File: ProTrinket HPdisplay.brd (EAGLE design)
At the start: 17.8 x 37.3 mm, 17 parts

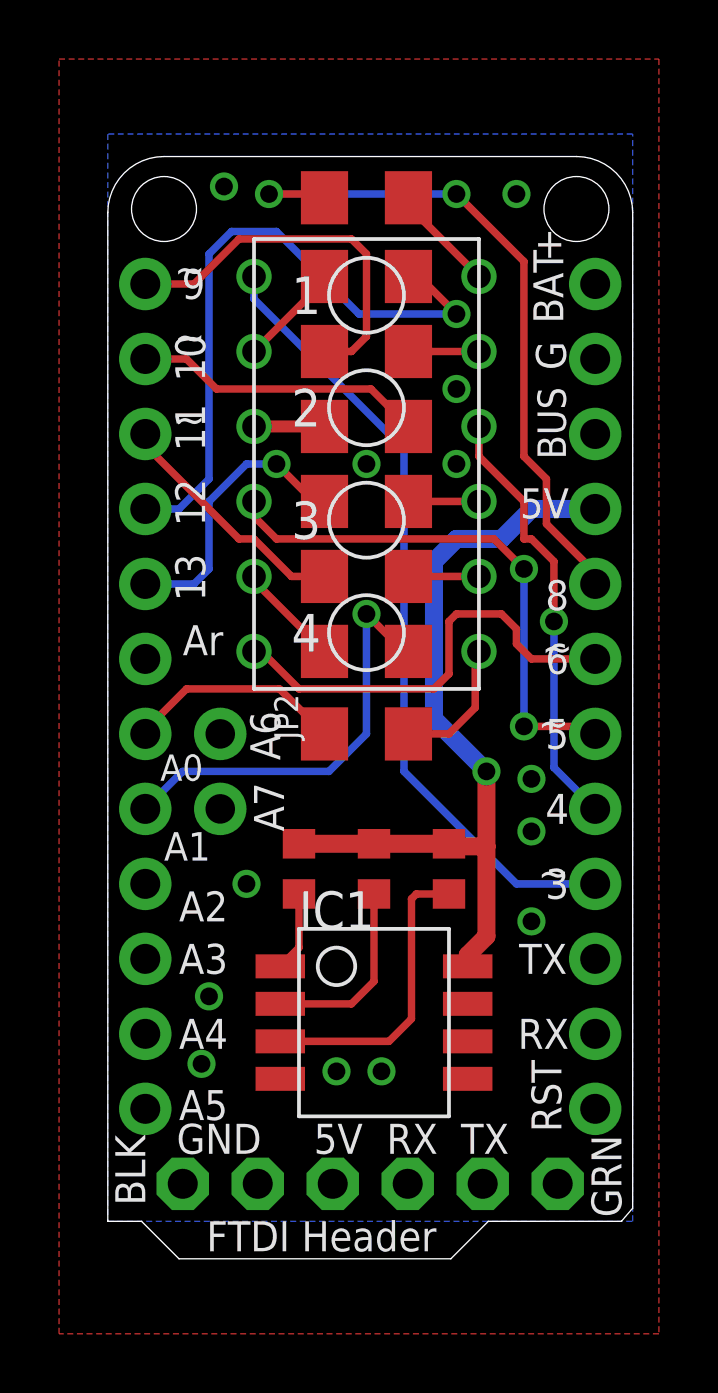
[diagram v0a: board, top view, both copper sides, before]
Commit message: fixed IIC connection
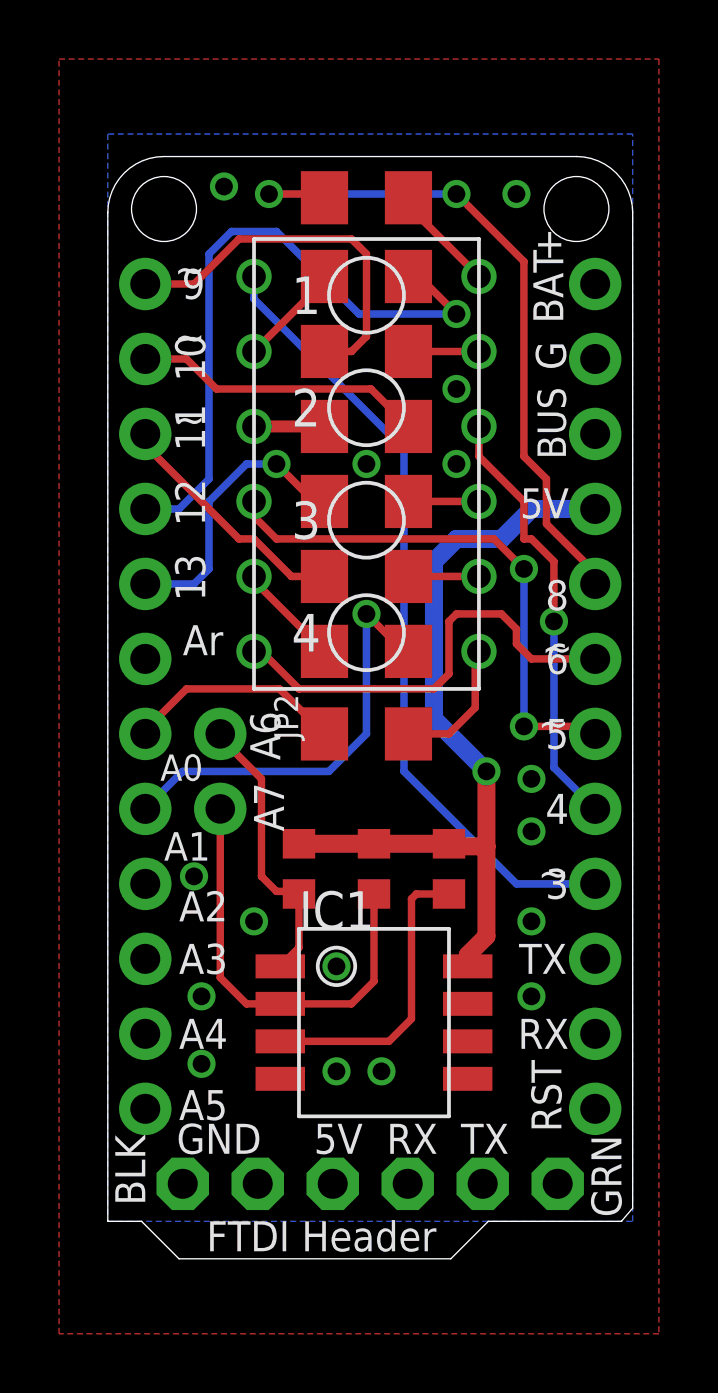
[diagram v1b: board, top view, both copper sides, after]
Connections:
- removed net N$10: IC1.2, R10.2
- removed net N$13: IC1.1, R9.2
- new net A6: IC1.1, JP2.1, R9.2
- new net A7: IC1.2, JP2.2, R10.2
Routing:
- net A7: track 0.00 -> 14.6 mm
- net A6: track 0.00 -> 9.64 mm
- net N$10: track 6.45 -> 0.00 mm
- net N$13: track 2.72 -> 0.00 mm
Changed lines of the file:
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@@
 <layer number="2" name="Route2" color="1" fill="3" visible="no" active="yes"/>
 <layer number="3" name="Route3" color="4" fill="3" visible="no" active="yes"/>
-<layer number="4" name="Route4" color="1" fill="4" visible="no" active="yes"/>
+<layer number="4" name="Route4" color="1" fill="4" visible="yes" active="yes"/>
 <layer number="5" name="Route5" color="4" fill="4" visible="no" active="yes"/>
 <layer number="6" name="Route6" color="1" fill="8" visible="no" active="yes"/>
@@
 <vertex x="12.7" y="33.02"/>
 </polygon>
-<via x="19.05" y="48.26" extent="1-16" drill="0.6"/>
+<via x="17.272" y="48.514" extent="1-16" drill="0.6"/>
 <via x="22.098" y="41.91" extent="1-16" drill="0.6"/>
 <via x="28.702" y="50.038" extent="1-16" drill="0.6"/>
-<via x="17.78" y="44.45" extent="1-16" drill="0.6"/>
+<via x="17.526" y="44.45" extent="1-16" drill="0.6"/>
 <via x="17.526" y="42.164" extent="1-16" drill="0.6"/>
 <via x="28.702" y="46.99" extent="1-16" drill="0.6"/>
@@
 <via x="26.162" y="62.484" extent="1-16" drill="0.6"/>
 <via x="23.114" y="62.484" extent="1-16" drill="0.6"/>
+<via x="19.304" y="46.99" extent="1-16" drill="0.6"/>
+<via x="22.098" y="45.466" extent="1-16" drill="0.6"/>
+<via x="28.702" y="44.45" extent="1-16" drill="0.6"/>
 </signal>
 <signal name="VBUS" class="1">
@@
 <wire x1="19.304" y1="58.522" x2="21.692" y2="56.134" width="0.254" layer="1"/>
 </signal>
-<signal name="N$10">
+<signal name="A7">
 <contactref element="IC1" pad="2"/>
 <contactref element="R10" pad="2"/>
@@
 <wire x1="23.368" y1="44.958" x2="22.606" y2="44.196" width="0.254" layer="1"/>
 <wire x1="22.606" y1="44.196" x2="20.193" y2="44.196" width="0.254" layer="1"/>
+<contactref element="JP2" pad="2"/>
+<wire x1="18.161" y1="50.8" x2="18.161" y2="45.085" width="0.254" layer="1"/>
+<wire x1="18.161" y1="45.085" x2="19.05" y2="44.196" width="0.254" layer="1"/>
+<wire x1="19.05" y1="44.196" x2="20.193" y2="44.196" width="0.254" layer="1"/>
 </signal>
 <signal name="N$11">
@@
 <wire x1="23.876" y1="42.926" x2="20.193" y2="42.926" width="0.254" layer="1"/>
 </signal>
-<signal name="N$13">
+<signal name="A6">
+<contactref element="JP2" pad="1"/>
 <contactref element="IC1" pad="1"/>
 <contactref element="R9" pad="2"/>
 <wire x1="20.828" y1="47.918" x2="20.828" y2="46.101" width="0.254" layer="1"/>
 <wire x1="20.828" y1="46.101" x2="20.193" y2="45.466" width="0.254" layer="1"/>
+<wire x1="18.161" y1="53.34" x2="18.161" y2="53.213" width="0.254" layer="1"/>
+<wire x1="18.161" y1="53.213" x2="19.558" y2="51.816" width="0.254" layer="1"/>
+<wire x1="19.558" y1="51.816" x2="19.558" y2="48.514" width="0.254" layer="1"/>
+<wire x1="19.558" y1="48.514" x2="20.066" y2="48.006" width="0.254" layer="1"/>
+<wire x1="20.066" y1="48.006" x2="20.74" y2="48.006" width="0.254" layer="1"/>
+<wire x1="20.74" y1="48.006" x2="20.828" y2="47.918" width="0.254" layer="1"/>
 </signal>
 </signals>

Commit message: removed vias
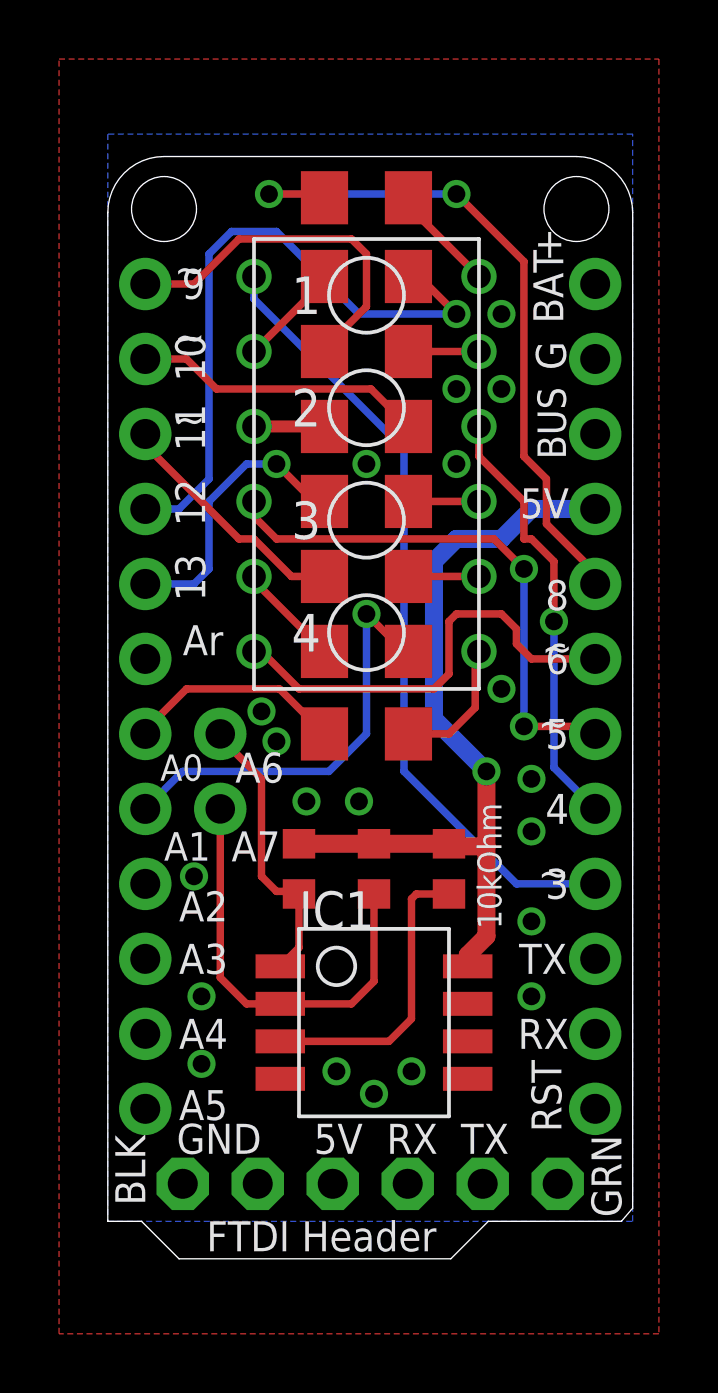
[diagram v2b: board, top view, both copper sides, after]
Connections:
- net GND: now also FTDI.2
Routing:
- net D9: track 12.8 -> 12.2 mm
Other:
- board text added: "10kOhm"
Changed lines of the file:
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@@
 <text x="16.764" y="45.72" size="1.016" layer="21" font="vector" ratio="10" rot="R180" align="center-right">A3</text>
 <text x="16.764" y="47.498" size="1.016" layer="21" font="vector" ratio="10" rot="R180" align="center-right">A2</text>
-<text x="19.812" y="50.038" size="1.016" layer="21" font="vector" ratio="10" rot="R270" align="center-right">A7</text>
+<text x="18.542" y="49.53" size="1.016" layer="21" font="vector" ratio="10" rot="R180" align="center-right">A7</text>
 <text x="16.256" y="49.53" size="0.9652" layer="21" font="vector" ratio="10" rot="R180" align="center-right">A1</text>
 <text x="16.129" y="52.197" size="0.889" layer="21" font="vector" ratio="10" rot="R180" align="center-right">A0</text>
-<text x="19.685" y="52.451" size="1.016" layer="21" font="vector" ratio="10" rot="R270" align="center-right">A6</text>
+<text x="18.669" y="52.197" size="1.016" layer="21" font="vector" ratio="10" rot="R180" align="center-right">A6</text>
 <text x="16.891" y="56.515" size="1.016" layer="21" font="vector" ratio="10" rot="R180" align="center-right">Ar</text>
 <text x="17.145" y="59.436" size="1.016" layer="21" font="vector" ratio="10" rot="R90" align="center-right">13</text>
@@
 <text x="21.59" y="36.322" size="1.016" layer="21" font="vector" ratio="12" align="center">FTDI Header</text>
 <text x="24.13" y="53.848" size="1.27" layer="26" font="vector" rot="MR90">#IStandWithAhmed</text>
+<text x="27.686" y="46.736" size="0.8128" layer="21" font="vector" rot="R90">10kOhm</text>
 </plain>
 <attributes>
@@
 </element>
 <element name="JP2" library="microbuilder" package="1X02_ROUND" value="" x="18.161" y="52.07" smashed="yes" rot="R270">
-<attribute name="NAME" x="19.9898" y="54.6862" size="0.8128" layer="25" ratio="18" rot="R270"/>
 <attribute name="VALUE" x="14.986" y="54.61" size="0.4064" layer="27" ratio="10" rot="R270"/>
 </element>
@@
 </element>
 <element name="R8" library="rcl" package="R1206" value="680Ohm" x="23.114" y="56.134" smashed="yes">
-<attribute name="VALUE" x="21.082" y="50.546" size="1.27" layer="27" font="vector"/>
+<attribute name="VALUE" x="26.416" y="52.578" size="0.8128" layer="27" font="vector" rot="R90"/>
 </element>
 <element name="IC1" library="lm75" package="SO8_LM75" value="" x="23.368" y="44.196" rot="R270"/>
@@
 <contactref element="IC1" pad="5"/>
 <contactref element="IC1" pad="4"/>
-<via x="23.622" y="41.91" extent="1-16" drill="0.6"/>
+<via x="24.638" y="41.91" extent="1-16" drill="0.6"/>
 <polygon width="0.4064" layer="1">
 <vertex x="12.7" y="76.2"/>
@@
 <via x="28.702" y="51.816" extent="1-16" drill="0.6"/>
 <via x="26.162" y="65.024" extent="1-16" drill="0.6"/>
-<via x="28.194" y="71.628" extent="1-16" drill="0.6"/>
-<via x="18.288" y="71.882" extent="1-16" drill="0.6"/>
 <via x="26.162" y="62.484" extent="1-16" drill="0.6"/>
 <via x="23.114" y="62.484" extent="1-16" drill="0.6"/>
-<via x="19.304" y="46.99" extent="1-16" drill="0.6"/>
-<via x="22.098" y="45.466" extent="1-16" drill="0.6"/>
 <via x="28.702" y="44.45" extent="1-16" drill="0.6"/>
+<via x="23.368" y="41.148" extent="1-16" drill="0.6"/>
+<contactref element="FTDI" pad="2"/>
+<via x="27.686" y="67.564" extent="1-16" drill="0.6"/>
+<via x="27.686" y="65.024" extent="1-16" drill="0.6"/>
+<via x="27.686" y="54.864" extent="1-16" drill="0.6"/>
+<via x="19.558" y="54.102" extent="1-16" drill="0.6"/>
+<via x="21.082" y="51.054" extent="1-16" drill="0.6"/>
+<via x="22.86" y="51.054" extent="1-16" drill="0.6"/>
+<via x="20.066" y="53.086" extent="1-16" drill="0.6"/>
 </signal>
 <signal name="VBUS" class="1">
@@
 <wire x1="18.796" y1="70.104" x2="22.606" y2="70.104" width="0.254" layer="1"/>
 <wire x1="22.606" y1="70.104" x2="23.114" y2="69.596" width="0.254" layer="1"/>
-<wire x1="23.114" y1="69.596" x2="23.114" y2="66.802" width="0.254" layer="1"/>
-<wire x1="23.114" y1="66.802" x2="22.606" y2="66.294" width="0.254" layer="1"/>
-<wire x1="22.606" y1="66.294" x2="21.692" y2="66.294" width="0.254" layer="1"/>
+<wire x1="23.114" y1="69.596" x2="23.114" y2="67.818" width="0.254" layer="1"/>
+<wire x1="23.114" y1="67.818" x2="22.352" y2="67.056" width="0.254" layer="1"/>
+<wire x1="22.352" y1="67.056" x2="21.692" y2="66.294" width="0.254" layer="1"/>
 </signal>
 <signal name="AREF">

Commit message: mixed up IIC lines
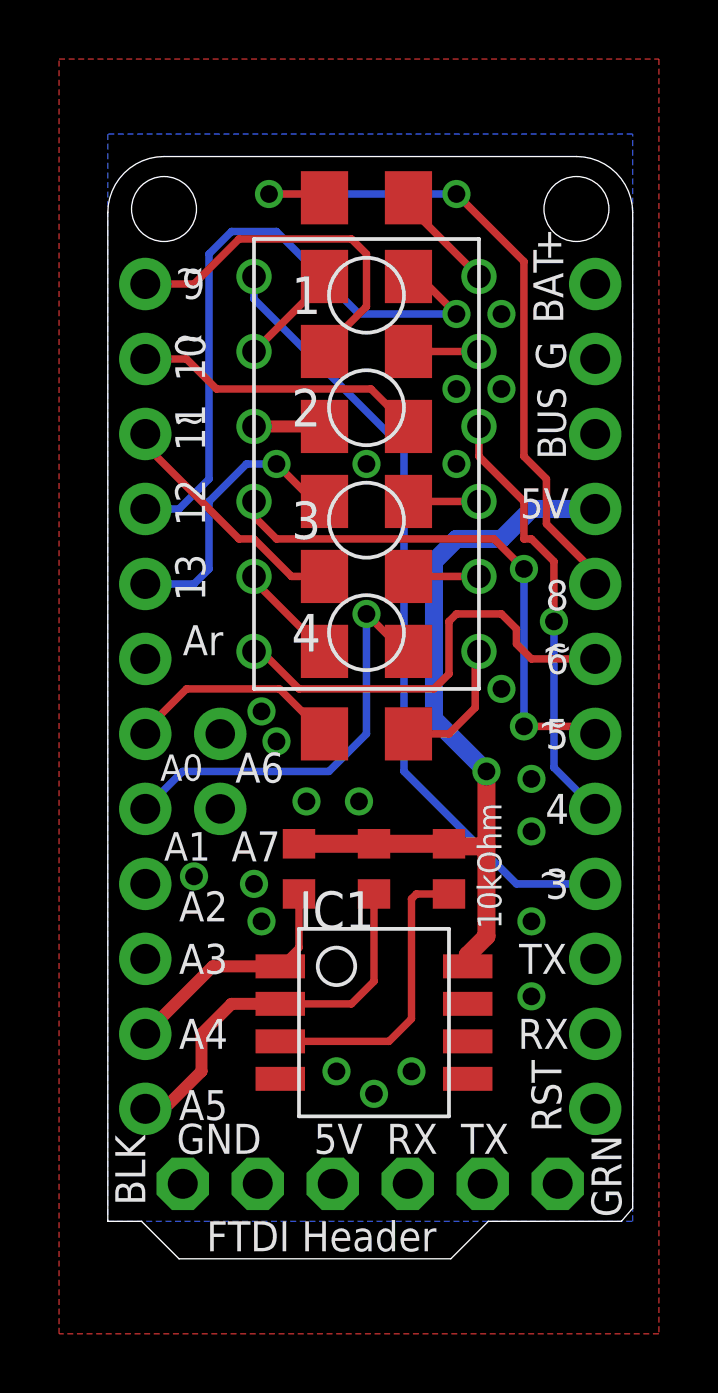
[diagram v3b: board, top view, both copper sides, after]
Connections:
- net A4: now also IC1.1, R9.2
- net A5: now also IC1.2, R10.2
- net A6: no longer IC1.1, R9.2
- net A7: no longer IC1.2, R10.2
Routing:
- net A7: track 14.6 -> 0.00 mm
- net A5: track 0.36 -> 13.2 mm
- net A6: track 9.64 -> 0.00 mm
- net A4: track 0.00 -> 8.23 mm
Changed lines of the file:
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@@
 <via x="22.098" y="41.91" extent="1-16" drill="0.6"/>
 <via x="28.702" y="50.038" extent="1-16" drill="0.6"/>
-<via x="17.526" y="44.45" extent="1-16" drill="0.6"/>
-<via x="17.526" y="42.164" extent="1-16" drill="0.6"/>
+<via x="19.304" y="48.26" extent="1-16" drill="0.6"/>
+<via x="19.558" y="46.99" extent="1-16" drill="0.6"/>
 <via x="28.702" y="46.99" extent="1-16" drill="0.6"/>
 <via x="28.702" y="51.816" extent="1-16" drill="0.6"/>
@@
 <signal name="A4">
 <contactref element="JP4" pad="11"/>
+<contactref element="IC1" pad="1"/>
+<contactref element="R9" pad="2"/>
+<wire x1="20.828" y1="47.918" x2="20.828" y2="46.101" width="0.254" layer="1"/>
+<wire x1="20.828" y1="46.101" x2="20.193" y2="45.466" width="0.254" layer="1"/>
+<wire x1="20.193" y1="45.466" x2="17.907" y2="45.466" width="0.4064" layer="1"/>
+<wire x1="17.907" y1="45.466" x2="15.621" y2="43.18" width="0.4064" layer="1"/>
 </signal>
 <signal name="A5">
 <contactref element="JP4" pad="12"/>
-<wire x1="15.875" y1="40.894" x2="15.621" y2="40.64" width="0.254" layer="16"/>
+<contactref element="IC1" pad="2"/>
+<contactref element="R10" pad="2"/>
+<wire x1="23.368" y1="47.918" x2="23.368" y2="44.958" width="0.254" layer="1"/>
+<wire x1="23.368" y1="44.958" x2="22.606" y2="44.196" width="0.254" layer="1"/>
+<wire x1="22.606" y1="44.196" x2="20.193" y2="44.196" width="0.254" layer="1"/>
+<wire x1="20.193" y1="44.196" x2="18.542" y2="44.196" width="0.4064" layer="1"/>
+<wire x1="18.542" y1="44.196" x2="17.526" y2="43.18" width="0.4064" layer="1"/>
+<wire x1="17.526" y1="43.18" x2="17.526" y2="41.91" width="0.4064" layer="1"/>
+<wire x1="17.526" y1="41.91" x2="16.256" y2="40.64" width="0.4064" layer="1"/>
+<wire x1="16.256" y1="40.64" x2="15.621" y2="40.64" width="0.4064" layer="1"/>
 </signal>
 <signal name="D3">
@@
 </signal>
 <signal name="A7">
-<contactref element="IC1" pad="2"/>
-<contactref element="R10" pad="2"/>
-<wire x1="23.368" y1="47.918" x2="23.368" y2="44.958" width="0.254" layer="1"/>
-<wire x1="23.368" y1="44.958" x2="22.606" y2="44.196" width="0.254" layer="1"/>
-<wire x1="22.606" y1="44.196" x2="20.193" y2="44.196" width="0.254" layer="1"/>
 <contactref element="JP2" pad="2"/>
-<wire x1="18.161" y1="50.8" x2="18.161" y2="45.085" width="0.254" layer="1"/>
-<wire x1="18.161" y1="45.085" x2="19.05" y2="44.196" width="0.254" layer="1"/>
-<wire x1="19.05" y1="44.196" x2="20.193" y2="44.196" width="0.254" layer="1"/>
 </signal>
 <signal name="N$11">
@@
 <signal name="A6">
 <contactref element="JP2" pad="1"/>
-<contactref element="IC1" pad="1"/>
-<contactref element="R9" pad="2"/>
-<wire x1="20.828" y1="47.918" x2="20.828" y2="46.101" width="0.254" layer="1"/>
-<wire x1="20.828" y1="46.101" x2="20.193" y2="45.466" width="0.254" layer="1"/>
-<wire x1="18.161" y1="53.34" x2="18.161" y2="53.213" width="0.254" layer="1"/>
-<wire x1="18.161" y1="53.213" x2="19.558" y2="51.816" width="0.254" layer="1"/>
-<wire x1="19.558" y1="51.816" x2="19.558" y2="48.514" width="0.254" layer="1"/>
-<wire x1="19.558" y1="48.514" x2="20.066" y2="48.006" width="0.254" layer="1"/>
-<wire x1="20.066" y1="48.006" x2="20.74" y2="48.006" width="0.254" layer="1"/>
-<wire x1="20.74" y1="48.006" x2="20.828" y2="47.918" width="0.254" layer="1"/>
 </signal>
 </signals>
